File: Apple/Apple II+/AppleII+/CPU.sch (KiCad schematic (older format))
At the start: 10 parts, among them U3 MOS6502

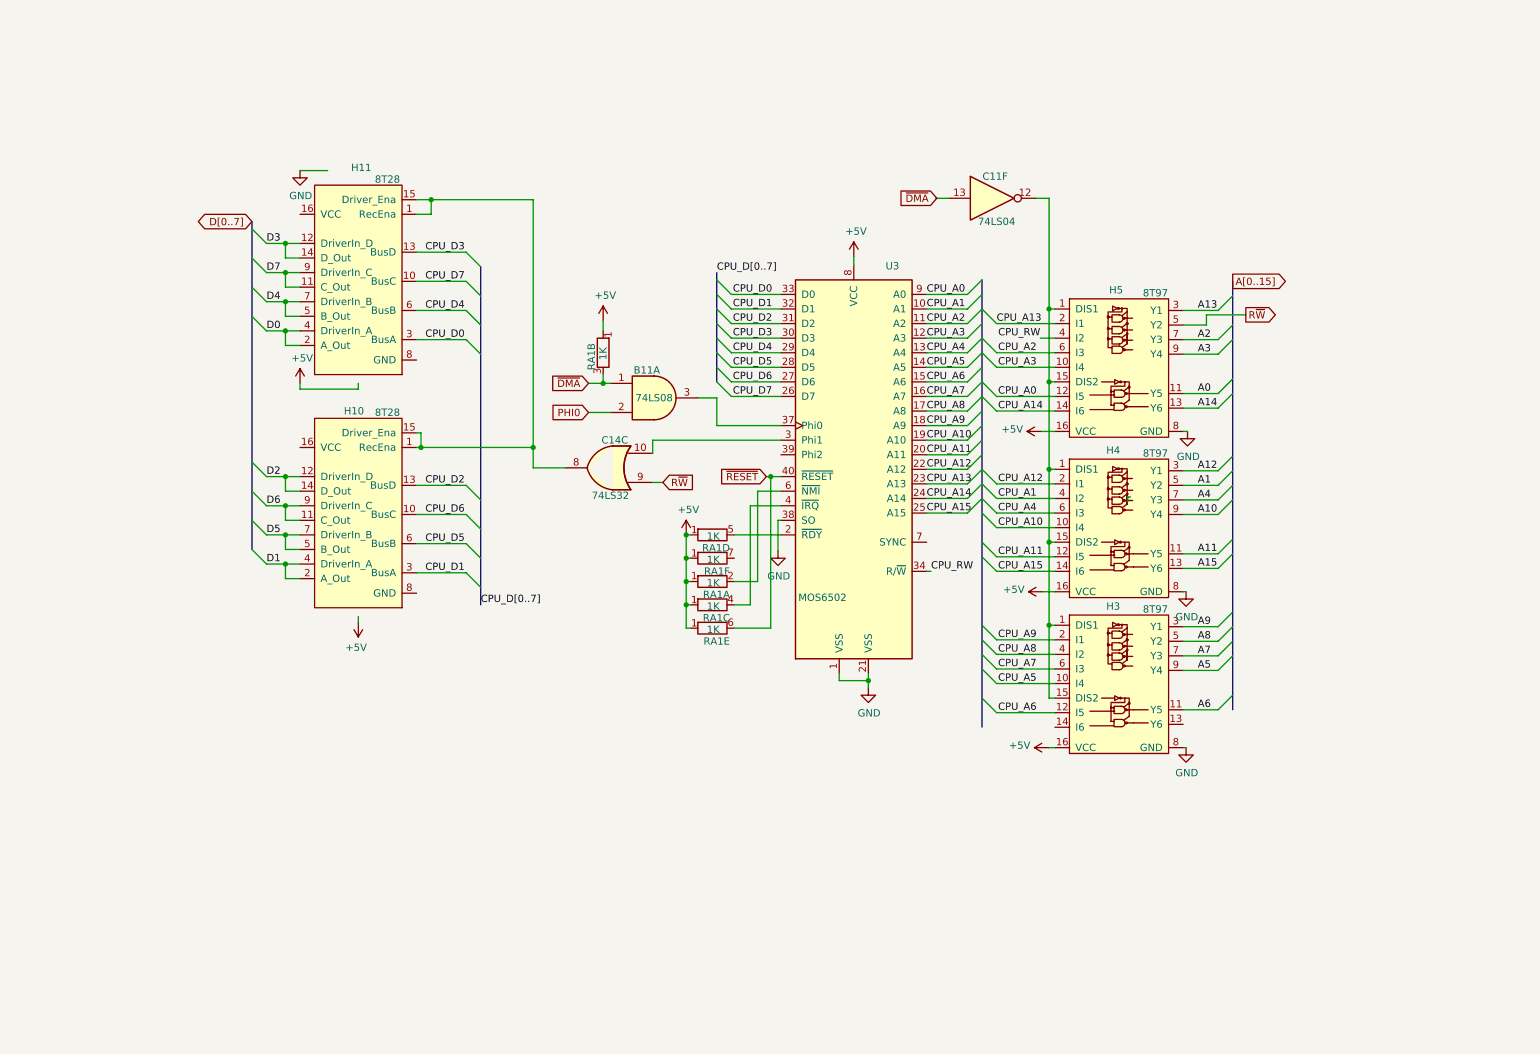
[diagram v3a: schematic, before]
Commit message: Additional updated to the Clock Generator Sheet, and the CPU sheet
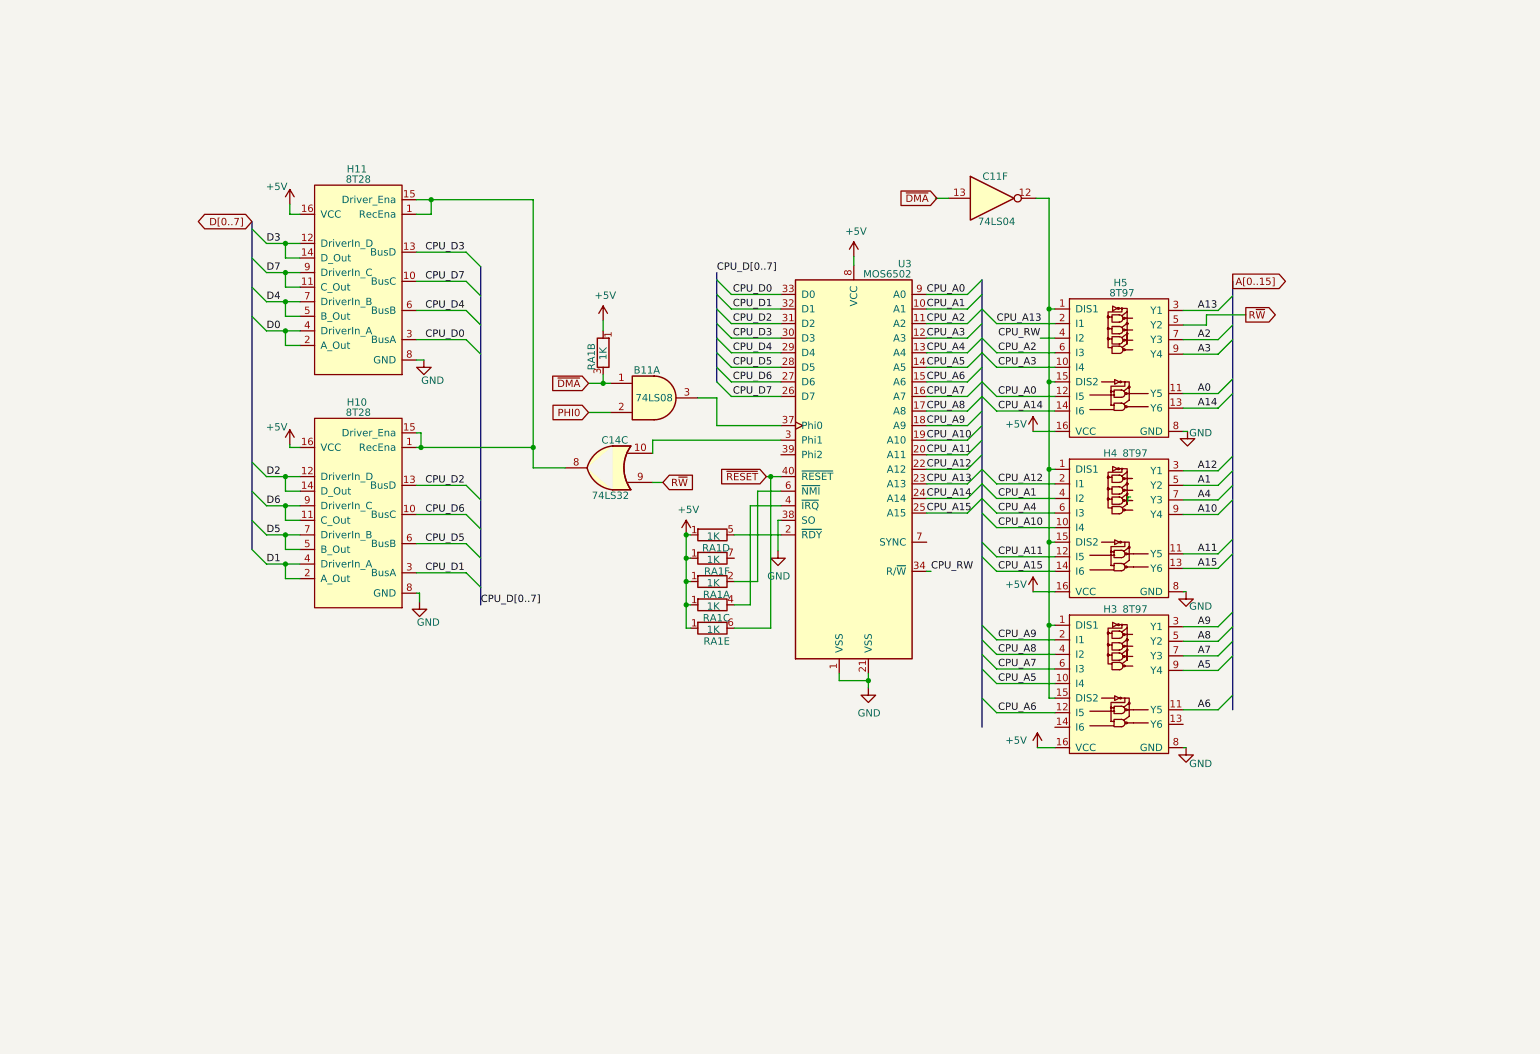
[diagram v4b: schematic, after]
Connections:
- wire segments 177 -> 179
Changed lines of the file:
@@
 encoding utf-8
 Sheet 2 8
-Title ""
+Title "Apple II+ Schematic"
 Date ""
 Rev ""
 Comp ""
-Comment1 ""
+Comment1 "Captured from the Apple II Reference Manual (1979)"
 Comment2 ""
 Comment3 ""
@@
 U 1 1 5FEA2C1D
 P 6470 3720
-F 0 "U3" H 6735 5115 50  0000 C CNN
-F 1 "MOS6502" H 6255 2840 50  0000 C CNN
+F 0 "U3" H 6820 5130 50  0000 C CNN
+F 1 "MOS6502" H 6700 5060 50  0000 C CNN
 F 2 "Package_DIP:DIP-40_W15.24mm" H 6470 2220 50  0001 C CNN
 F 3 "http://pdf.datasheetcatalog.com/datasheet/motorola/MC68A00L.pdf" H 6470 3720 50  0001 C CNN
@@
 U 1 1 600920C0
 P 8250 4000
-F 0 "H4" H 8250 4410 50  0000 C CNN
-F 1 "8T97" H 8540 4390 50  0000 C CNN
+F 0 "H4" H 8230 4390 50  0000 C CNN
+F 1 "8T97" H 8400 4390 50  0000 C CNN
 F 2 "" H 8280 4000 50  0001 C CNN
 F 3 "" H 8280 4000 50  0001 C CNN
@@
 U 1 1 600CA7E7
 P 8250 5070
-F 0 "H3" H 8250 5480 50  0000 C CNN
-F 1 "8T97" H 8540 5460 50  0000 C CNN
+F 0 "H3" H 8230 5460 50  0000 C CNN
+F 1 "8T97" H 8400 5460 50  0000 C CNN
 F 2 "" H 8280 5070 50  0001 C CNN
 F 3 "" H 8280 5070 50  0001 C CNN
@@
 U 1 1 60056C39
 P 8250 2900
-F 0 "H5" H 8270 3310 50  0000 C CNN
-F 1 "8T97" H 8540 3290 50  0000 C CNN
+F 0 "H5" H 8300 3360 50  0000 C CNN
+F 1 "8T97" H 8310 3290 50  0000 C CNN
 F 2 "" H 8280 2900 50  0001 C CNN
 F 3 "" H 8280 2900 50  0001 C CNN
@@
 U 1 1 6006D96A
 P 3070 2470
-F 0 "H11" H 3050 1650 50  0000 C CNN
-F 1 "8T28" H 2870 1730 50  0000 C CNN
+F 0 "H11" H 3080 1660 50  0000 C CNN
+F 1 "8T28" H 3070 1730 50  0000 C CNN
 F 2 "" H 3070 2470 50  0001 C CNN
 F 3 "" H 3070 2470 50  0001 C CNN
@@
 U 1 1 60075353
 P 3070 4070
-F 0 "H10" H 3100 3320 50  0000 C CNN
-F 1 "8T28" H 2870 3330 50  0000 C CNN
+F 0 "H10" H 3080 3260 50  0000 C CNN
+F 1 "8T28" H 3070 3330 50  0000 C CNN
 F 2 "" H 3070 4070 50  0001 C CNN
 F 3 "" H 3070 4070 50  0001 C CNN
@@
 	2340 2670 2440 2770
 $Comp
-L power:+5V #PWR0117
-U 1 1 60218C74
-P 3070 4770
-F 0 "#PWR0117" H 3070 4620 50  0001 C CNN
-F 1 "+5V" H 3085 4943 50  0000 C CNN
-F 2 "" H 3070 4770 50  0001 C CNN
-F 3 "" H 3070 4770 50  0001 C CNN
-	1    3070 4770
-	-1   0    0    1
-$EndComp
-Wire Wire Line
-	3070 4730 3070 4770
-$Comp
-L power:+5V #PWR0118
-U 1 1 60225858
-P 2670 3130
-F 0 "#PWR0118" H 2670 2980 50  0001 C CNN
-F 1 "+5V" H 2685 3303 50  0000 C CNN
-F 2 "" H 2670 3130 50  0001 C CNN
-F 3 "" H 2670 3130 50  0001 C CNN
-	1    2670 3130
-	1    0    0    -1
-$EndComp
-Wire Wire Line
-	2670 3170 2670 3130
-Wire Wire Line
-	2670 3170 3070 3170
-Wire Wire Line
-	3070 3170 3070 3130
-$Comp
 L power:GND #PWR0119
 U 1 1 60236924
-P 2670 1670
-F 0 "#PWR0119" H 2670 1420 50  0001 C CNN
-F 1 "GND" H 2675 1497 50  0000 C CNN
-F 2 "" H 2670 1670 50  0001 C CNN
-F 3 "" H 2670 1670 50  0001 C CNN
-	1    2670 1670
-	1    0    0    -1
-$EndComp
-Wire Wire Line
-	2670 1670 2860 1670
+P 3520 2970
+F 0 "#PWR0119" H 3520 2720 50  0001 C CNN
+F 1 "GND" H 3580 2830 50  0000 C CNN
+F 2 "" H 3520 2970 50  0001 C CNN
+F 3 "" H 3520 2970 50  0001 C CNN
+	1    3520 2970
+	1    0    0    -1
+$EndComp
 Wire Wire Line
 	4270 3570 3500 3570
@@
 P 8750 5630
 F 0 "#PWR?" H 8750 5380 50  0001 C CNN
-F 1 "GND" H 8755 5457 50  0000 C CNN
+F 1 "GND" H 8850 5520 50  0000 C CNN
 F 2 "" H 8750 5630 50  0001 C CNN
 F 3 "" H 8750 5630 50  0001 C CNN
@@
 P 8750 4560
 F 0 "#PWR?" H 8750 4310 50  0001 C CNN
-F 1 "GND" H 8755 4387 50  0000 C CNN
+F 1 "GND" H 8850 4460 50  0000 C CNN
 F 2 "" H 8750 4560 50  0001 C CNN
 F 3 "" H 8750 4560 50  0001 C CNN
@@
 P 8760 3460
 F 0 "#PWR?" H 8760 3210 50  0001 C CNN
-F 1 "GND" H 8765 3287 50  0000 C CNN
+F 1 "GND" H 8850 3450 50  0000 C CNN
 F 2 "" H 8760 3460 50  0001 C CNN
 F 3 "" H 8760 3460 50  0001 C CNN
@@
 L power:+5V #PWR?
 U 1 1 6008DD62
-P 7760 3460
-F 0 "#PWR?" H 7760 3310 50  0001 C CNN
-F 1 "+5V" V 7775 3588 50  0000 L CNN
-F 2 "" H 7760 3460 50  0001 C CNN
-F 3 "" H 7760 3460 50  0001 C CNN
-	1    7760 3460
-	0    -1   -1   0
-$EndComp
-Wire Wire Line
-	7760 3460 7850 3460
+P 7700 3460
+F 0 "#PWR?" H 7700 3310 50  0001 C CNN
+F 1 "+5V" H 7510 3510 50  0000 L CNN
+F 2 "" H 7700 3460 50  0001 C CNN
+F 3 "" H 7700 3460 50  0001 C CNN
+	1    7700 3460
+	1    0    0    -1
+$EndComp
+Wire Wire Line
+	7700 3460 7850 3460
 $Comp
 L power:+5V #PWR?
 U 1 1 60099357
-P 7770 4560
-F 0 "#PWR?" H 7770 4410 50  0001 C CNN
-F 1 "+5V" V 7785 4688 50  0000 L CNN
-F 2 "" H 7770 4560 50  0001 C CNN
-F 3 "" H 7770 4560 50  0001 C CNN
-	1    7770 4560
-	0    -1   -1   0
-$EndComp
-Wire Wire Line
-	7770 4560 7850 4560
+P 7700 4560
+F 0 "#PWR?" H 7700 4410 50  0001 C CNN
+F 1 "+5V" H 7510 4610 50  0000 L CNN
+F 2 "" H 7700 4560 50  0001 C CNN
+F 3 "" H 7700 4560 50  0001 C CNN
+	1    7700 4560
+	1    0    0    -1
+$EndComp
+Wire Wire Line
+	7700 4560 7850 4560
 $Comp
 L power:+5V #PWR?
 U 1 1 600B0A85
-P 7810 5630
-F 0 "#PWR?" H 7810 5480 50  0001 C CNN
-F 1 "+5V" V 7825 5758 50  0000 L CNN
-F 2 "" H 7810 5630 50  0001 C CNN
-F 3 "" H 7810 5630 50  0001 C CNN
-	1    7810 5630
-	0    -1   -1   0
-$EndComp
-Wire Wire Line
-	7810 5630 7850 5630
+P 7730 5630
+F 0 "#PWR?" H 7730 5480 50  0001 C CNN
+F 1 "+5V" H 7510 5680 50  0000 L CNN
+F 2 "" H 7730 5630 50  0001 C CNN
+F 3 "" H 7730 5630 50  0001 C CNN
+	1    7730 5630
+	1    0    0    -1
+$EndComp
+Wire Wire Line
+	7730 5630 7850 5630
 Wire Wire Line
 	4490 3710 4270 3710
@@
 Wire Wire Line
 	5900 3770 5970 3770
+Wire Wire Line
+	3470 2970 3520 2970
+$Comp
+L power:+5V #PWR0118
+U 1 1 60225858
+P 2600 1900
+F 0 "#PWR0118" H 2600 1750 50  0001 C CNN
+F 1 "+5V" H 2510 2020 50  0000 C CNN
+F 2 "" H 2600 1900 50  0001 C CNN
+F 3 "" H 2600 1900 50  0001 C CNN
+	1    2600 1900
+	1    0    0    -1
+$EndComp
+Wire Wire Line
+	2600 1900 2600 1970
+Wire Wire Line
+	2600 1970 2670 1970
+$Comp
+L power:+5V #PWR?
+U 1 1 6025E1E7
+P 2600 3550
+F 0 "#PWR?" H 2600 3400 50  0001 C CNN
+F 1 "+5V" H 2510 3670 50  0000 C CNN
+F 2 "" H 2600 3550 50  0001 C CNN
+F 3 "" H 2600 3550 50  0001 C CNN
+	1    2600 3550
+	1    0    0    -1
+$EndComp
+$Comp
+L power:GND #PWR?
+U 1 1 6025E888
+P 3490 4630
+F 0 "#PWR?" H 3490 4380 50  0001 C CNN
+F 1 "GND" H 3550 4490 50  0000 C CNN
+F 2 "" H 3490 4630 50  0001 C CNN
+F 3 "" H 3490 4630 50  0001 C CNN
+	1    3490 4630
+	1    0    0    -1
+$EndComp
+Wire Wire Line
+	2600 3550 2600 3570
+Wire Wire Line
+	2600 3570 2670 3570
+Wire Wire Line
+	3470 4570 3490 4570
+Wire Wire Line
+	3490 4570 3490 4630
 Wire Bus Line
 	3910 2330 3910 4650

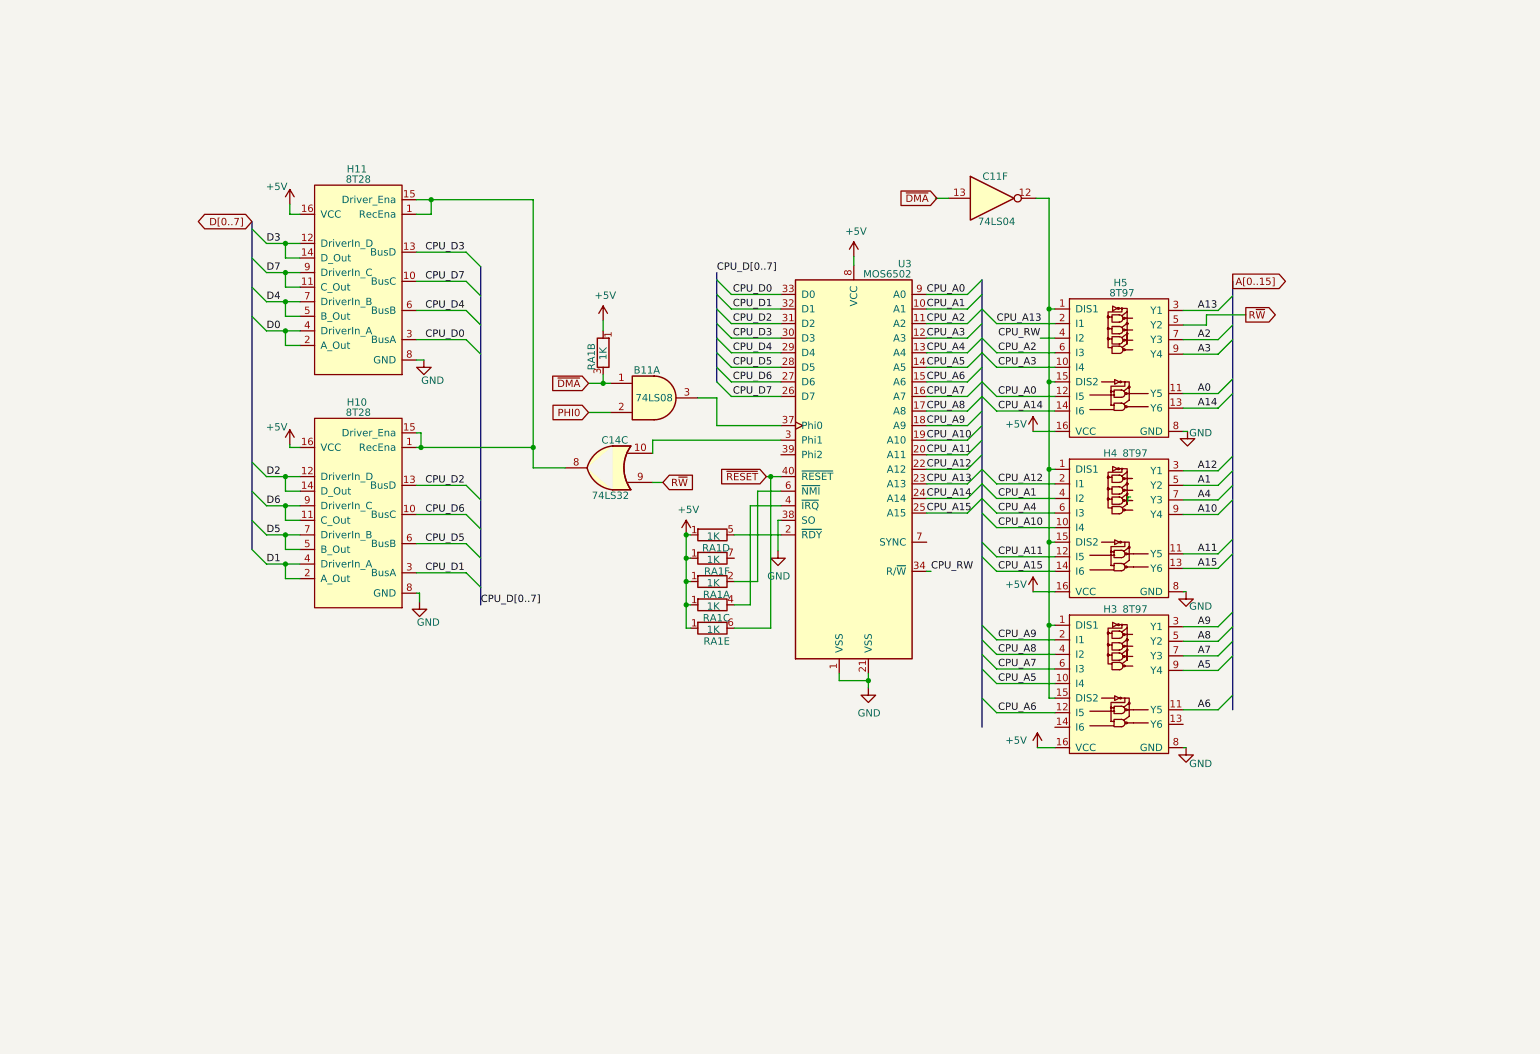
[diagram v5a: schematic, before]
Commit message: Added video generation sheet
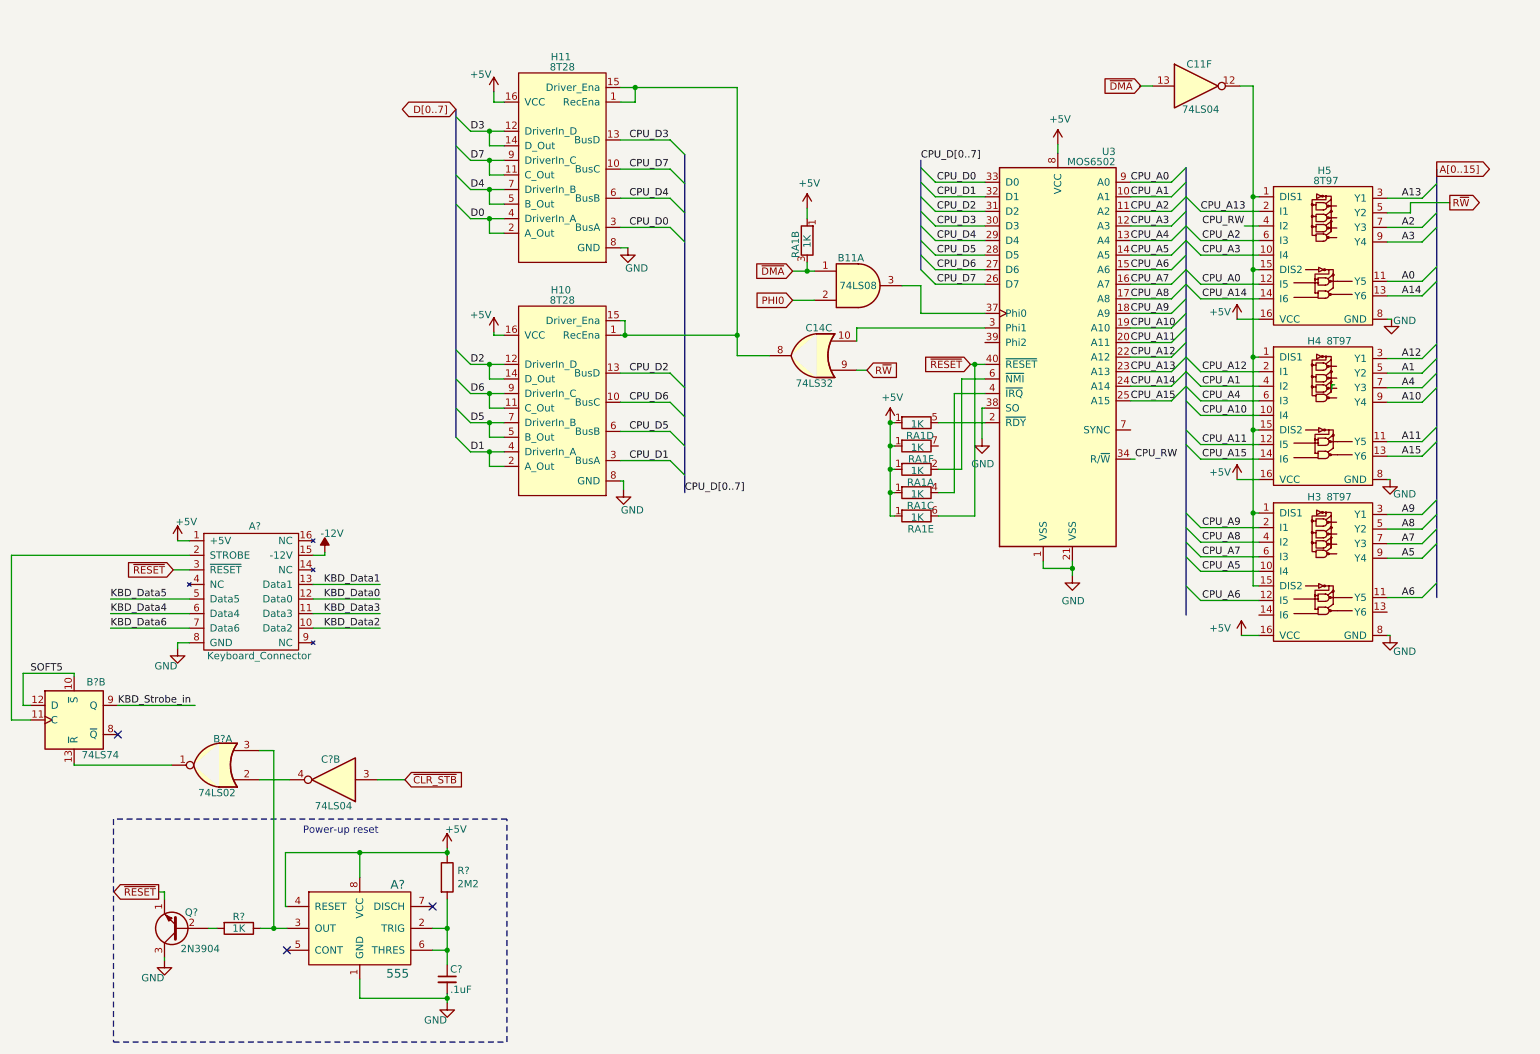
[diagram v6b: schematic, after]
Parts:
- added A?: 555, digikey-footprints:DIP-8_W7.62mm, symbol AppleII+:555
- added A?: Keyboard_Connector, symbol AppleII+:AppleII+_Keyboard_Connector
- added B?: 74LS74, symbol 74xx:74LS74
- added B?: 74LS02, symbol 74xx:74LS02
- added C?: 74LS04, symbol 74xx:74LS04
- added C?: .1uF, symbol Device:C_Small
- added Q?: 2N3904, Package_TO_SOT_THT:TO-92_Inline, symbol Transistor_BJT:2N3904
- added R?: 2M2, symbol Device:R
- added R?: 1K, symbol Device:R
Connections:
- net labels added: -12V, KBD_Data0, KBD_Data1, KBD_Data2, KBD_Data3, KBD_Data4, KBD_Data5, KBD_Data6, KBD_Strobe_in, SOFT5, ~CLR_STB
- wire segments 179 -> 228
- no-connect marks 0 -> 3
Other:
- note added: "Power-up reset"
- moved on the sheet: B11A, C11F, C14C, H10, H11, H3, H4, H5, RA1A, RA1B, RA1C, RA1D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

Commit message: updated additional sheets, and Readme.md
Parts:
- added B6, B7: 74LS257, symbol 74xx:74LS257
- gave numbers to parts that had none: 9
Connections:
- net labels added: LD0, LD1, LD2, LD3, LD4, LD5, LD6, LD7, ~KBD, ~RAM_SEL
- net labels removed: KBD_Strobe_in
- wire segments 228 -> 258
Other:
- moved on the sheet: B11A, C11B, C11F, C14C, H3, H4, H5, RA1A, RA1B, RA1C, RA1D, RA1E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
